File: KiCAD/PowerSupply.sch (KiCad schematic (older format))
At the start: 13 parts, among them J2 USB_Micro_B, J3 Binder 709 Female Panel Mount, Q1 3.7A, 30V, U2 AP2112K-3.3, U3 LM1117

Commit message: Redoing layout
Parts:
- removed J3: Binder 709 Female Panel Mount, Pin_Headers:Pin_Header_Straight_1x04_Pitch2.54mm, symbol Conn_01x04
- added J3: Battery Headers, Pin_Headers:Pin_Header_Straight_1x02_Pitch2.54mm, symbol Conn_01x02
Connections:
- net +BATT: now also J3.1 (Pin_1)
- net GND: now also J3.2 (Pin_2)
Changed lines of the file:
@@
 	1    0    0    -1
 $EndComp
-$Comp
-L Conn_01x04 J3
-U 1 1 5C661C12
-P 4500 4600
-F 0 "J3" H 4500 4800 50  0000 C CNN
-F 1 "Binder 709 Female Panel Mount" H 4500 4300 50  0001 C CNN
-F 2 "Pin_Headers:Pin_Header_Straight_1x04_Pitch2.54mm" H 4500 4600 50  0001 C CNN
-F 3 "" H 4500 4600 50  0001 C CNN
-	1    4500 4600
-	-1   0    0    -1
-$EndComp
-Text GLabel 4900 4500 2    39   Input ~ 0
-CANH
-Text GLabel 4900 4600 2    39   Input ~ 0
-CANL
-Text Notes 4475 4275 0    49   ~ 0
+Text Notes 4375 4295 0    49   ~ 0
 Binder Series 709 Female \nPanel Mount Connector
 $Comp
@@
 Wire Wire Line
 	5925 5100 5925 5000
-Wire Wire Line
-	4700 4700 5625 4700
 Wire Wire Line
 	6225 4800 6275 4800
@@
 	4400 3100 4700 3100
 Wire Wire Line
-	4700 4500 4900 4500
-Wire Wire Line
-	4700 4600 4900 4600
-Wire Wire Line
-	5325 4800 4700 4800
-Wire Wire Line
 	4675 2900 4675 3000
 Connection ~ 4675 3000
+$Comp
+L Conn_01x02 J3
+U 1 1 5C9D06F2
+P 4845 4700
+F 0 "J3" H 4845 4800 50  0000 C CNN
+F 1 "Battery Headers" H 4845 4500 50  0001 C CNN
+F 2 "Pin_Headers:Pin_Header_Straight_1x02_Pitch2.54mm" H 4845 4700 50  0001 C CNN
+F 3 "" H 4845 4700 50  0001 C CNN
+	1    4845 4700
+	-1   0    0    -1
+$EndComp
+Wire Wire Line
+	5045 4700 5625 4700
+Wire Wire Line
+	5325 4800 5045 4800
 $EndSCHEMATC

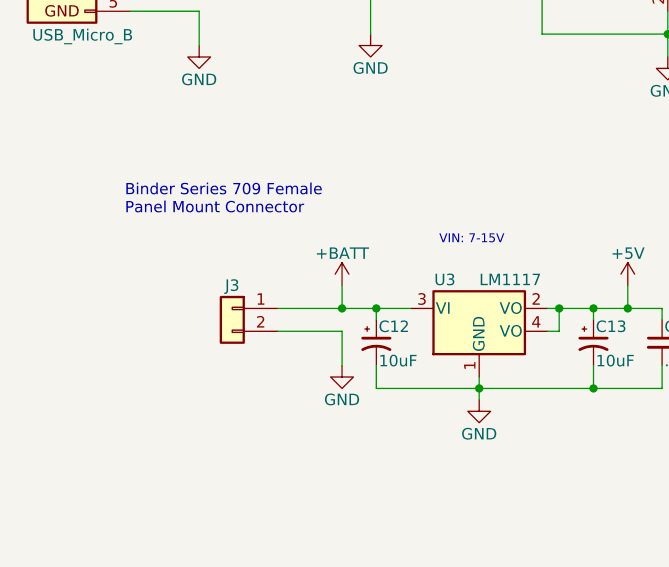
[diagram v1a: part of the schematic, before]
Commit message: Dropped 4 spare sensors, revising layout.
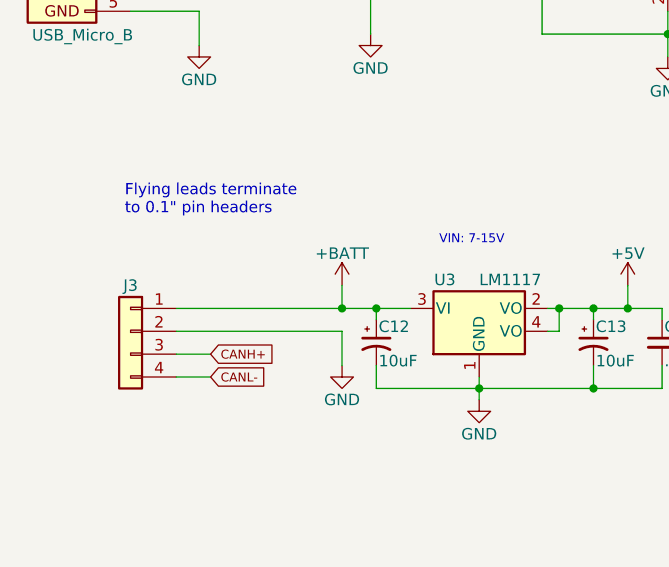
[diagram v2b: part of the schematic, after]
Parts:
- removed J3: Battery Headers, Pin_Headers:Pin_Header_Straight_1x02_Pitch2.54mm, symbol Conn_01x02
- added J3: Conn_01x04, Pin_Headers:Pin_Header_Straight_1x04_Pitch2.54mm, symbol Conn_01x04
- C10, C11, C9: footprint Capacitors_SMD:C_1210 -> Capacitors_SMD:C_0603
- C14: footprint Capacitors_SMD:C_1206 -> Capacitors_SMD:C_0603
- R5: footprint Resistors_SMD:R_1210 -> Resistors_SMD:R_0603
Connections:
- net +BATT: now also J3.1 (Pin_1)
- net GND: now also J3.2 (Pin_2)
- new net CANH+: J3.3 (Pin_3)
- new net CANL-: J3.4 (Pin_4)
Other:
- note added: "Flying leads terminate\nto 0.1" pin headers"
- note removed: "Binder Series 709 Female \nPanel Mount Connector"
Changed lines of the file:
@@
 F 0 "C14" H 6735 4920 50  0000 L CNN
 F 1 ".1uF" H 6735 4770 50  0000 L CNN
-F 2 "Capacitors_SMD:C_1206" H 6725 4850 50  0001 C CNN
+F 2 "Capacitors_SMD:C_0603" H 6725 4850 50  0001 C CNN
 F 3 "" H 6725 4850 50  0001 C CNN
 	1    6725 4850
@@
 F 0 "R5" V 5580 2350 50  0000 C CNN
 F 1 "10k" V 5500 2350 50  0000 C CNN
-F 2 "Resistors_SMD:R_1210" V 5430 2350 50  0001 C CNN
+F 2 "Resistors_SMD:R_0603" V 5430 2350 50  0001 C CNN
 F 3 "" H 5500 2350 50  0001 C CNN
 	1    5500 2350
@@
 F 0 "C11" H 7235 3270 50  0000 L CNN
 F 1 "2.2uF" H 7235 3120 50  0000 L CNN
-F 2 "Capacitors_SMD:C_1210" H 7225 3200 50  0001 C CNN
+F 2 "Capacitors_SMD:C_0603" H 7225 3200 50  0001 C CNN
 F 3 "" H 7225 3200 50  0001 C CNN
 	1    7225 3200
@@
 F 0 "C10" H 6210 3270 50  0000 L CNN
 F 1 "1.0uF" H 6210 3120 50  0000 L CNN
-F 2 "Capacitors_SMD:C_1210" H 6200 3200 50  0001 C CNN
+F 2 "Capacitors_SMD:C_0603" H 6200 3200 50  0001 C CNN
 F 3 "" H 6200 3200 50  0001 C CNN
 	1    6200 3200
@@
 F 0 "C9" H 5460 3270 50  0000 L CNN
 F 1 "2.2uF" H 5460 3120 50  0000 L CNN
-F 2 "Capacitors_SMD:C_1210" H 5450 3200 50  0001 C CNN
+F 2 "Capacitors_SMD:C_0603" H 5450 3200 50  0001 C CNN
 F 3 "" H 5450 3200 50  0001 C CNN
 	1    5450 3200
@@
 $EndComp
 Text Notes 4375 4295 0    49   ~ 0
-Binder Series 709 Female \nPanel Mount Connector
+Flying leads terminate\nto 0.1" pin headers
 $Comp
 L USB_Micro_B J2
@@
 Connection ~ 4675 3000
 $Comp
-L Conn_01x02 J3
-U 1 1 5C9D06F2
-P 4845 4700
-F 0 "J3" H 4845 4800 50  0000 C CNN
-F 1 "Battery Headers" H 4845 4500 50  0001 C CNN
-F 2 "Pin_Headers:Pin_Header_Straight_1x02_Pitch2.54mm" H 4845 4700 50  0001 C CNN
-F 3 "" H 4845 4700 50  0001 C CNN
-	1    4845 4700
+L Conn_01x04 J3
+U 1 1 5D288B5A
+P 4400 4800
+F 0 "J3" H 4400 5000 50  0000 C CNN
+F 1 "Conn_01x04" H 4400 4500 50  0001 C CNN
+F 2 "Pin_Headers:Pin_Header_Straight_1x04_Pitch2.54mm" H 4400 4800 50  0001 C CNN
+F 3 "" H 4400 4800 50  0001 C CNN
+	1    4400 4800
 	-1   0    0    -1
 $EndComp
 Wire Wire Line
-	5045 4700 5625 4700
-Wire Wire Line
-	5325 4800 5045 4800
+	5625 4700 4600 4700
+Wire Wire Line
+	5325 4800 4600 4800
+Text GLabel 4750 4900 2    39   Input ~ 0
+CANH+
+Text GLabel 4750 5000 2    39   Input ~ 0
+CANL-
+Wire Wire Line
+	4750 4900 4600 4900
+Wire Wire Line
+	4600 5000 4750 5000
 $EndSCHEMATC

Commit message: Finished layout V0.01
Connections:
- net CANH+ renamed CAN+
- net CANL- renamed CAN-
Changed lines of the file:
@@
 	5325 4800 4600 4800
 Text GLabel 4750 4900 2    39   Input ~ 0
-CANH+
+CAN+
 Text GLabel 4750 5000 2    39   Input ~ 0
-CANL-
+CAN-
 Wire Wire Line
 	4750 4900 4600 4900

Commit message: Change NPTH Mounting holes and swap to JST PH Series Connector
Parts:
- J3: footprint Pin_Headers:Pin_Header_Straight_1x04_Pitch2.54mm -> Connectors_JST:JST_PH_B4B-PH-K_04x2.00mm_Straight
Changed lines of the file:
@@
 F 0 "J3" H 4400 5000 50  0000 C CNN
 F 1 "Conn_01x04" H 4400 4500 50  0001 C CNN
-F 2 "Pin_Headers:Pin_Header_Straight_1x04_Pitch2.54mm" H 4400 4800 50  0001 C CNN
+F 2 "Connectors_JST:JST_PH_B4B-PH-K_04x2.00mm_Straight" H 4400 4800 50  0001 C CNN
 F 3 "" H 4400 4800 50  0001 C CNN
 	1    4400 4800
